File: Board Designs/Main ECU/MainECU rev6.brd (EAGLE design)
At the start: 120.6 x 78.9 mm, 194 parts, among them J1 JUMPER, J2 JUMPER, J3 JUMPER, J4 JUMPER, J5 JUMPER, J6 JUMPER, J7 JUMPER, J8 JUMPER, Q1 P-CHANNEL_MOSFET_DMP3099L-7, Q12 P-CHANNEL_MOSFET_DMP3099L-7, X1 CONNECTOR-37, X2 CONNECTOR-4AUTOSPORT, X3 CONNECTOR-4NANO-FIT-VERTICAL-4, X4 CONNECTOR-4NANO-FIT-VERTICAL-4

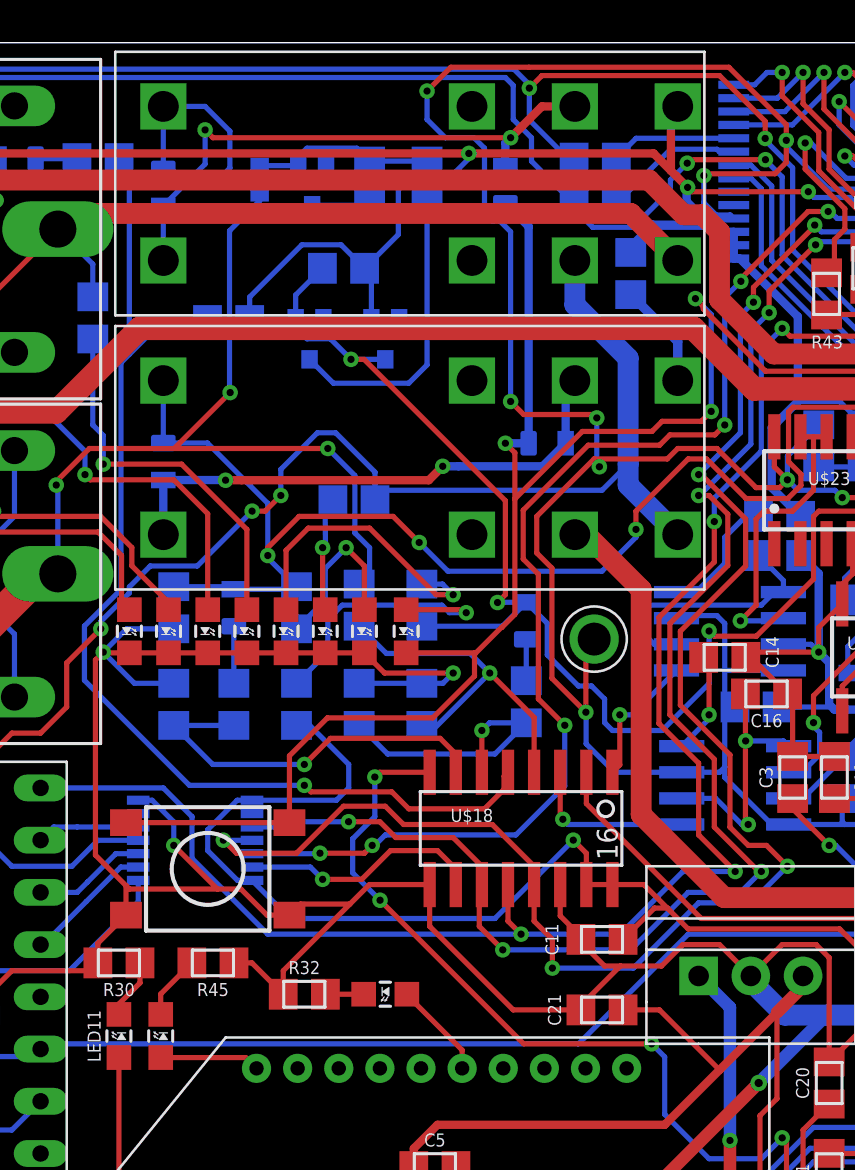
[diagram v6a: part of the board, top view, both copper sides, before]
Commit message: Main ECU rev5/6: Move level shifter OE pin to VCCA
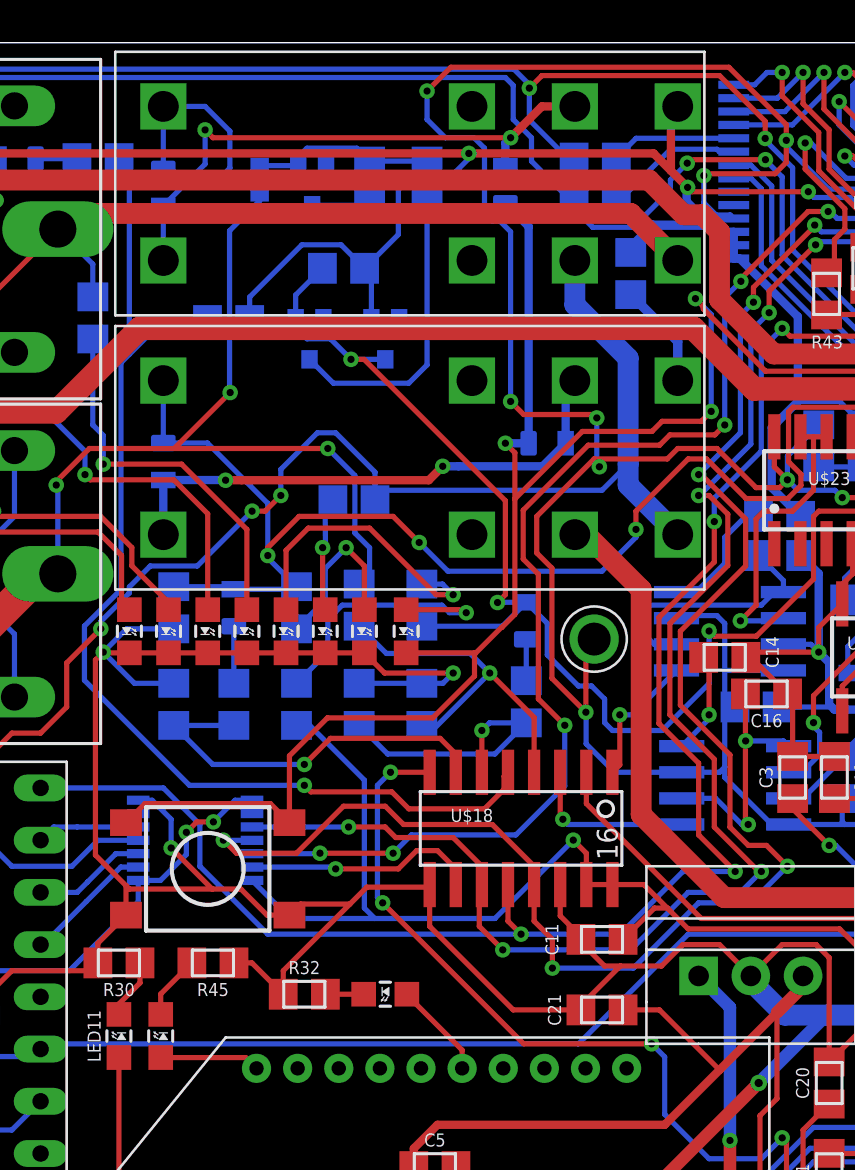
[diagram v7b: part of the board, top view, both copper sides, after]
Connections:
- net +5V: no longer U$25.8
- net 3.3V_MAIN_TEENSY: now also U$25.8
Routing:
- net 3.3V_MAIN_TEENSY: track 34.4 -> 42.2 mm, vias 1 -> 3
- net +5V: track 362.2 -> 357.6 mm
- net TEMPSENSE: track 108.2 -> 106.9 mm
- net LATCH_EXT_BUTTON: track 91.1 -> 91.8 mm

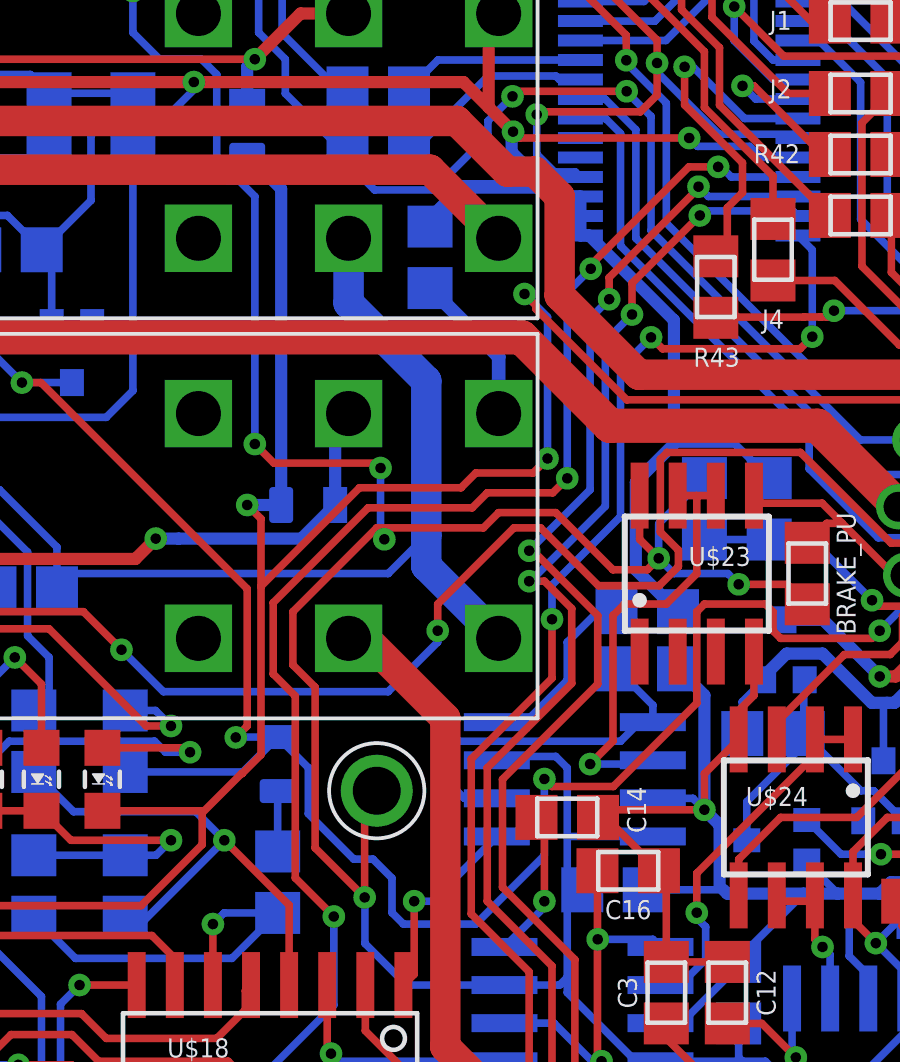
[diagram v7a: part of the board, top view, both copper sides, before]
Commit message: Main ECU rev5/6: Add CAN label to connector
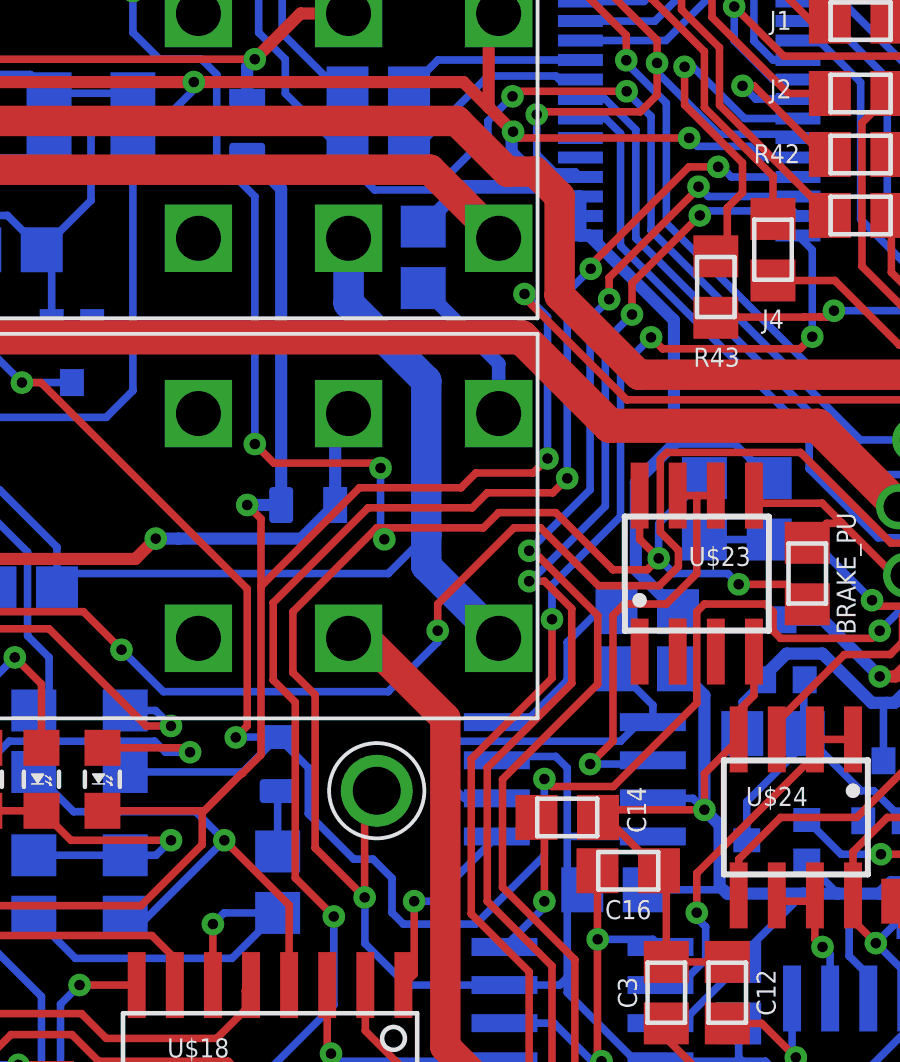
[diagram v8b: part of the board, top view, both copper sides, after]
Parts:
- moved R63 0.23 mm to (47.3, 67.7)
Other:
- board text added: "CAN"
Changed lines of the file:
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@@
 <setting verticaltext="up"/>
 </settings>
-<grid distance="5" unitdist="mil" unit="mil" style="lines" multiple="1" display="yes" altdistance="5" altunitdist="mil" altunit="mil"/>
+<grid distance="1" unitdist="mil" unit="mil" style="lines" multiple="1" display="yes" altdistance="5" altunitdist="mil" altunit="mil"/>
 <layers>
 <layer number="1" name="Top" color="4" fill="1" visible="yes" active="yes"/>
@@
 <text x="20.574" y="40.005" size="0.8128" layer="51" font="vector" rot="R90" align="top-center">Shutdown Latch</text>
 <text x="24.638" y="0.635" size="0.762" layer="51" font="vector">Updates by Nathan Cheek, Soohyun Kim, Arvind Srinivasan</text>
+<text x="81.407" y="48.514" size="1.016" layer="51" font="vector" rot="R270" align="bottom-center">CAN</text>
 </plain>
 <attributes>
@@
 <attribute name="VALUE" x="45.7708" y="74.0156" size="0.3048" layer="28" rot="MR180" align="top-center"/>
 </element>
-<element name="R63" library="HyTechDevices" package="0805" value="" x="47.498" y="67.691" smashed="yes" rot="MR90">
-<attribute name="NAME" x="47.498" y="65.8241" size="0.635" layer="26" font="vector" rot="MR180" align="bottom-center"/>
-<attribute name="VALUE" x="46.7868" y="67.691" size="0.3048" layer="28" rot="MR90" align="top-center"/>
+<element name="R63" library="HyTechDevices" package="0805" value="" x="47.2694" y="67.691" smashed="yes" rot="MR90">
+<attribute name="NAME" x="47.2694" y="65.8241" size="0.635" layer="26" font="vector" rot="MR180" align="bottom-center"/>
+<attribute name="VALUE" x="46.5582" y="67.691" size="0.3048" layer="28" rot="MR90" align="top-center"/>
 </element>
 </elements>
@@
 <wire x1="48.5775" y1="70.0405" x2="51.3715" y2="70.0405" width="0.4572" layer="16"/>
 <contactref element="R63" pad="2"/>
-<wire x1="47.498" y1="68.716" x2="47.498" y2="68.961" width="0.4572" layer="16"/>
-<wire x1="47.498" y1="68.961" x2="48.5775" y2="70.0405" width="0.4572" layer="16"/>
+<wire x1="47.2694" y1="68.716" x2="47.2694" y2="68.7324" width="0.4572" layer="16"/>
+<wire x1="47.2694" y1="68.7324" x2="48.5775" y2="70.0405" width="0.4572" layer="16"/>
 <wire x1="50.2158" y1="71.1962" x2="50.2158" y2="71.8312" width="0.4064" layer="16"/>
 <wire x1="50.2158" y1="71.8312" x2="50.264403125" y2="71.879803125" width="0.4064" layer="16"/>
@@
 <wire x1="74.168" y1="43.688" x2="77.216" y2="46.736" width="0.254" layer="1"/>
 <wire x1="74.168" y1="35.306" x2="74.168" y2="43.688" width="0.254" layer="1"/>
-<wire x1="42.926" y1="54.102" x2="43.6654" y2="53.3626" width="0.254" layer="1"/>
-<wire x1="43.6654" y1="53.3626" x2="43.6654" y2="48.006" width="0.254" layer="1"/>
+<wire x1="42.926" y1="53.848" x2="43.6654" y2="53.1086" width="0.254" layer="1"/>
+<wire x1="43.6654" y1="53.1086" x2="43.6654" y2="48.006" width="0.254" layer="1"/>
 <contactref element="C4" pad="1"/>
 <contactref element="U$27" pad="4"/>
@@
 <contactref element="U$26" pad="4"/>
 <contactref element="U$26" pad="7"/>
-<wire x1="42.926" y1="54.102" x2="42.926" y2="55.88" width="0.254" layer="1"/>
+<wire x1="42.926" y1="53.848" x2="42.926" y2="55.88" width="0.254" layer="1"/>
 <wire x1="51.689" y1="59.182" x2="49.784" y2="59.182" width="0.254" layer="1"/>
 <wire x1="61.214" y1="34.036" x2="61.214" y2="34.29" width="0.254" layer="16"/>
@@
 <wire x1="51.4124" y1="65.70260625" x2="50.645403125" y2="66.469603125" width="0.254" layer="16"/>
 <via x="50.645403125" y="66.469603125" extent="1-16" drill="0.35"/>
-<wire x1="50.645403125" y1="66.469603125" x2="51.0286" y2="66.08640625" width="0.254" layer="1"/>
-<wire x1="51.0286" y1="66.08640625" x2="51.0286" y2="65.96784375" width="0.254" layer="1"/>
+<wire x1="54.05524375" y1="62.9412" x2="50.645403125" y2="66.351040625" width="0.254" layer="1"/>
+<wire x1="50.645403125" y1="66.469603125" x2="50.645403125" y2="66.351040625" width="0.254" layer="1"/>
 <wire x1="50.93018125" y1="60.5028" x2="49.022" y2="60.5028" width="0.254" layer="1"/>
-<wire x1="51.0286" y1="65.96784375" x2="54.05524375" y2="62.9412" width="0.254" layer="1"/>
 <contactref element="X1" pad="P$37"/>
 <wire x1="64.72733125" y1="62.23" x2="64.01613125" y2="62.9412" width="0.254" layer="1"/>
@@
 <wire x1="51.5874" y1="59.8424" x2="49.403" y2="59.8424" width="0.254" layer="1"/>
 <wire x1="45.43263125" y1="59.34236875" x2="42.2684" y2="56.1781375" width="0.254" layer="1"/>
-<wire x1="42.2684" y1="56.1781375" x2="42.2684" y2="53.8038625" width="0.254" layer="1"/>
-<wire x1="42.2684" y1="53.8038625" x2="43.005" y2="53.0672625" width="0.254" layer="1"/>
+<wire x1="42.2684" y1="56.1781375" x2="42.2684" y2="53.6006625" width="0.254" layer="1"/>
+<wire x1="42.2684" y1="53.6006625" x2="43.005" y2="52.8640625" width="0.254" layer="1"/>
 <wire x1="43.005" y1="47.0041" x2="44.2891" y2="45.72" width="0.254" layer="1"/>
 <via x="44.2891" y="45.72" extent="1-16" drill="0.35"/>
 <via x="35.941" y="39.497" extent="1-16" drill="0.35"/>
-<wire x1="43.005" y1="53.0672625" x2="43.005" y2="47.0041" width="0.254" layer="1"/>
+<wire x1="43.005" y1="52.8640625" x2="43.005" y2="47.0041" width="0.254" layer="1"/>
 <wire x1="57.2008" y1="70.7066" x2="57.0992" y2="70.7066" width="0.254" layer="16"/>
 <wire x1="29.0798" y1="39.4745" x2="32.3625" y2="39.4745" width="0.254" layer="16"/>
@@
 <contactref element="IMD_SHUTDOWN_RLY" pad="4"/>
 <contactref element="R63" pad="1"/>
-<wire x1="49.784" y1="64.38" x2="47.498" y2="66.666" width="0.4572" layer="16"/>
-<wire x1="49.784" y1="62.484" x2="49.784" y2="64.38" width="0.4572" layer="16"/>
+<wire x1="49.784" y1="64.1514" x2="47.2694" y2="66.666" width="0.4572" layer="16"/>
+<wire x1="49.784" y1="62.484" x2="49.784" y2="64.1514" width="0.4572" layer="16"/>
 </signal>
 <signal name="DASH_11_OPT">
